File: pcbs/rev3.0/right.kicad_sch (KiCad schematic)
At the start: 31 parts, among them J2 Conn_ST_STDC14, SW66 MK-12C03-G015, U10 GT-TC020A-H035-L05, U6 LDI1117, U7 USBLC6-2SC6_C5261088, U8 358, U9 STM32F446RCTx, Y2 8MHz

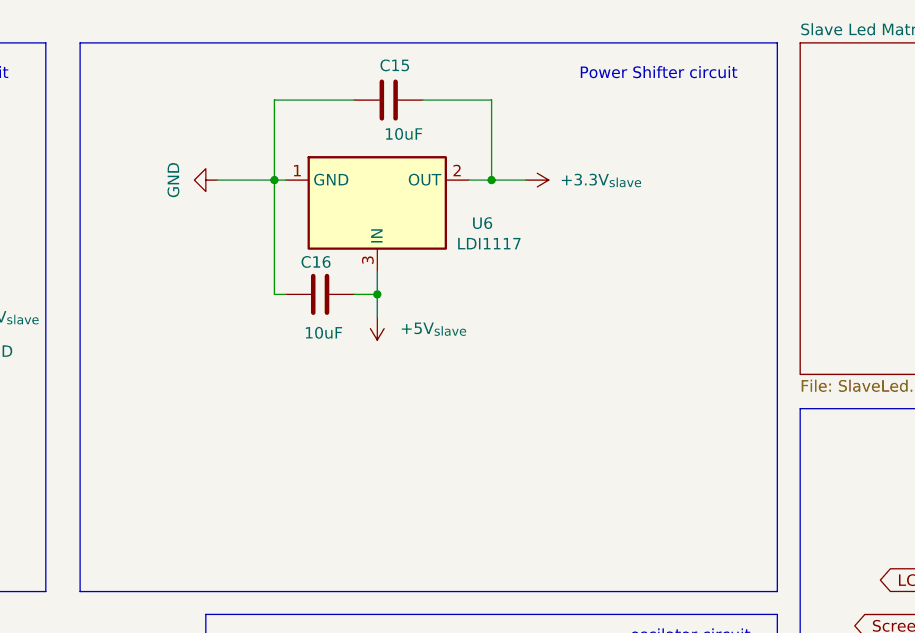
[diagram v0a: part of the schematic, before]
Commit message: Change LDI3.3 LCSC part number to Diotec part
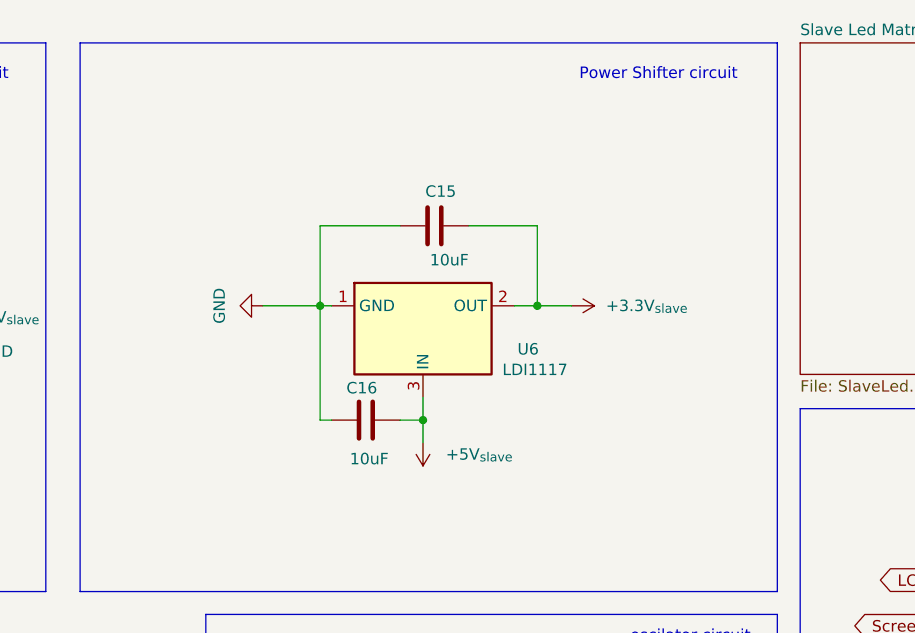
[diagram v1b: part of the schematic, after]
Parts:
- U6: LCSC C6186 -> (none); LCSC Part C6186 -> (none)
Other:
- moved on the sheet: C15, C16, U6
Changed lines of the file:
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@@
 	)
 	(junction
-		(at 157.48 43.18)
+		(at 162.56 57.15)
 		(diameter 0)
 		(color 0 0 0 0)
@@
 	)
 	(junction
-		(at 146.05 30.48)
+		(at 151.13 44.45)
 		(diameter 0)
 		(color 0 0 0 0)
@@
 	)
 	(junction
-		(at 170.18 30.48)
+		(at 175.26 44.45)
 		(diameter 0)
 		(color 0 0 0 0)
@@
 	(wire
 		(pts
-			(xy 157.48 45.72) (xy 157.48 43.18)
+			(xy 162.56 59.69) (xy 162.56 57.15)
 		)
 		(stroke
@@
 	(wire
 		(pts
-			(xy 146.05 43.18) (xy 147.32 43.18)
+			(xy 151.13 57.15) (xy 152.4 57.15)
 		)
 		(stroke
@@
 	(wire
 		(pts
-			(xy 167.64 30.48) (xy 170.18 30.48)
+			(xy 172.72 44.45) (xy 175.26 44.45)
 		)
 		(stroke
@@
 	(wire
 		(pts
-			(xy 146.05 21.59) (xy 146.05 30.48)
+			(xy 151.13 35.56) (xy 151.13 44.45)
 		)
 		(stroke
@@
 	(wire
 		(pts
-			(xy 154.94 21.59) (xy 146.05 21.59)
+			(xy 160.02 35.56) (xy 151.13 35.56)
 		)
 		(stroke
@@
 	(wire
 		(pts
-			(xy 157.48 43.18) (xy 157.48 40.64)
+			(xy 162.56 57.15) (xy 162.56 54.61)
 		)
 		(stroke
@@
 	(wire
 		(pts
-			(xy 170.18 30.48) (xy 170.18 21.59)
+			(xy 175.26 44.45) (xy 175.26 35.56)
 		)
 		(stroke
@@
 	(wire
 		(pts
-			(xy 170.18 21.59) (xy 162.56 21.59)
+			(xy 175.26 35.56) (xy 167.64 35.56)
 		)
 		(stroke
@@
 	(wire
 		(pts
-			(xy 146.05 30.48) (xy 147.32 30.48)
+			(xy 151.13 44.45) (xy 152.4 44.45)
 		)
 		(stroke
@@
 	(wire
 		(pts
-			(xy 139.7 30.48) (xy 146.05 30.48)
+			(xy 144.78 44.45) (xy 151.13 44.45)
 		)
 		(stroke
@@
 	(wire
 		(pts
-			(xy 146.05 30.48) (xy 146.05 43.18)
+			(xy 151.13 44.45) (xy 151.13 57.15)
 		)
 		(stroke
@@
 	(wire
 		(pts
-			(xy 154.94 43.18) (xy 157.48 43.18)
+			(xy 160.02 57.15) (xy 162.56 57.15)
 		)
 		(stroke
@@
 	(wire
 		(pts
-			(xy 170.18 30.48) (xy 173.99 30.48)
+			(xy 175.26 44.45) (xy 179.07 44.45)
 		)
 		(stroke
@@
 	(symbol
 		(lib_id "Device:C")
-		(at 151.13 43.18 90)
+		(at 156.21 57.15 90)
 		(unit 1)
 		(exclude_from_sim no)
@@
 		(dnp no)
 		(property "Reference" "C16"
-			(at 152.4 39.624 90)
+			(at 157.48 53.594 90)
 			(effects
 				(font
@@
 		)
 		(property "Value" "10uF"
-			(at 153.67 47.498 90)
+			(at 158.75 61.468 90)
 			(effects
 				(font
@@
 		)
 		(property "Footprint" "Capacitor_SMD:C_1206_3216Metric"
-			(at 154.94 42.2148 0)
+			(at 160.02 56.1848 0)
 			(effects
 				(font
@@
 		)
 		(property "Datasheet" "~"
-			(at 151.13 43.18 0)
+			(at 156.21 57.15 0)
 			(effects
 				(font
@@
 		)
 		(property "Description" "Unpolarized capacitor"
-			(at 151.13 43.18 0)
+			(at 156.21 57.15 0)
 			(effects
 				(font
@@
 		)
 		(property "LCSC" "C13585"
-			(at 151.13 43.18 0)
+			(at 156.21 57.15 0)
 			(effects
 				(font
@@
 		)
 		(property "LCSC Part" "C13585"
-			(at 151.13 43.18 0)
+			(at 156.21 57.15 0)
 			(effects
 				(font
@@
 	(symbol
 		(lib_id "power:+3.3V")
-		(at 173.99 30.48 270)
+		(at 179.07 44.45 270)
 		(unit 1)
 		(exclude_from_sim no)
@@
 		(fields_autoplaced yes)
 		(property "Reference" "#PWR038"
-			(at 170.18 30.48 0)
+			(at 175.26 44.45 0)
 			(effects
 				(font
@@
 		)
 		(property "Value" "+3.3V_{slave}"
-			(at 177.8 30.4799 90)
+			(at 182.88 44.4499 90)
 			(effects
 				(font
@@
 		)
 		(property "Footprint" ""
-			(at 173.99 30.48 0)
+			(at 179.07 44.45 0)
 			(effects
 				(font
@@
 		)
 		(property "Datasheet" ""
-			(at 173.99 30.48 0)
+			(at 179.07 44.45 0)
 			(effects
 				(font
@@
 		)
 		(property "Description" "Power symbol creates a global label with name \"+3.3V\""
-			(at 173.99 30.48 0)
+			(at 179.07 44.45 0)
 			(effects
 				(font
@@
 	(symbol
 		(lib_id "Regulator_Linear:LT1963AxST-3.3")
-		(at 157.48 33.02 0)
+		(at 162.56 46.99 0)
 		(unit 1)
 		(exclude_from_sim no)
@@
 		(dnp no)
 		(property "Reference" "U6"
-			(at 169.164 35.306 0)
+			(at 174.244 49.276 0)
 			(effects
 				(font
@@
 		)
 		(property "Value" "LDI1117"
-			(at 169.926 37.592 0)
+			(at 175.006 51.562 0)
 			(effects
 				(font
@@
 		)
 		(property "Footprint" "Package_TO_SOT_SMD:SOT-223-3_TabPin2"
-			(at 157.48 44.45 0)
+			(at 162.56 58.42 0)
 			(effects
 				(font
@@
 			)
 		)
-		(property "Datasheet" "https://www.lcsc.com/datasheet/C6186.pdf"
-			(at 157.48 46.99 0)
+		(property "Datasheet" ""
+			(at 162.56 60.96 0)
 			(effects
 				(font
@@
 			)
 		)
-		(property "Description" "Advanced Monolithic Systems AMS1117-3.3"
-			(at 157.48 33.02 0)
+		(property "Description" ""
+			(at 162.56 46.99 0)
 			(effects
 				(font
@@
 			)
 		)
-		(property "LCSC" "C6186"
-			(at 157.48 33.02 0)
+		(property "LCSC" ""
+			(at 162.56 46.99 0)
 			(effects
 				(font
@@
 			)
 		)
-		(property "LCSC Part" "C6186"
-			(at 157.48 33.02 0)
+		(property "LCSC Part" ""
+			(at 162.56 46.99 0)
 			(effects
 				(font
@@
 	(symbol
 		(lib_id "Device:C")
-		(at 158.75 21.59 270)
+		(at 163.83 35.56 270)
 		(unit 1)
 		(exclude_from_sim no)
@@
 		(dnp no)
 		(property "Reference" "C15"
-			(at 157.734 17.78 90)
+			(at 162.814 31.75 90)
 			(effects
 				(font
@@
 		)
 		(property "Value" "10uF"
-			(at 158.242 25.4 90)
+			(at 163.322 39.37 90)
 			(effects
 				(font
@@
 		)
 		(property "Footprint" "Capacitor_SMD:C_1206_3216Metric"
-			(at 154.94 22.5552 0)
+			(at 160.02 36.5252 0)
 			(effects
 				(font
@@
 		)
 		(property "Datasheet" "~"
-			(at 158.75 21.59 0)
+			(at 163.83 35.56 0)
 			(effects
 				(font
@@
 		)
 		(property "Description" "Unpolarized capacitor"
-			(at 158.75 21.59 0)
+			(at 163.83 35.56 0)
 			(effects
 				(font
@@
 		)
 		(property "LCSC" "C13585"
-			(at 158.75 21.59 0)
+			(at 163.83 35.56 0)
 			(effects
 				(font
@@
 		)
 		(property "LCSC Part" "C13585"
-			(at 158.75 21.59 0)
+			(at 163.83 35.56 0)
 			(effects
 				(font
@@
 	(symbol
 		(lib_id "power:+5V")
-		(at 157.48 45.72 180)
+		(at 162.56 59.69 180)
 		(unit 1)
 		(exclude_from_sim no)
@@
 		(fields_autoplaced yes)
 		(property "Reference" "#PWR043"
-			(at 157.48 41.91 0)
+			(at 162.56 55.88 0)
 			(effects
 				(font
@@
 		)
 		(property "Value" "+5V_{slave}"
-			(at 160.02 46.9899 0)
+			(at 165.1 60.9599 0)
 			(effects
 				(font
@@
 		)
 		(property "Footprint" ""
-			(at 157.48 45.72 0)
+			(at 162.56 59.69 0)
 			(effects
 				(font
@@
 		)
 		(property "Datasheet" ""
-			(at 157.48 45.72 0)
+			(at 162.56 59.69 0)
 			(effects
 				(font
@@
 		)
 		(property "Description" "Power symbol creates a global label with name \"+5V\""
-			(at 157.48 45.72 0)
+			(at 162.56 59.69 0)
 			(effects
 				(font
@@
 	(symbol
 		(lib_id "power:GND")
-		(at 139.7 30.48 270)
+		(at 144.78 44.45 270)
 		(unit 1)
 		(exclude_from_sim no)
@@
 		(dnp no)
 		(property "Reference" "#PWR037"
-			(at 133.35 30.48 0)
+			(at 138.43 44.45 0)
 			(effects
 				(font
@@
 		)
 		(property "Value" "GND"
-			(at 134.874 30.48 0)
+			(at 139.954 44.45 0)
 			(effects
 				(font
@@
 		)
 		(property "Footprint" ""
-			(at 139.7 30.48 0)
+			(at 144.78 44.45 0)
 			(effects
 				(font
@@
 		)
 		(property "Datasheet" ""
-			(at 139.7 30.48 0)
+			(at 144.78 44.45 0)
 			(effects
 				(font
@@
 		)
 		(property "Description" "Power symbol creates a global label with name \"GND\" , ground"
-			(at 139.7 30.48 0)
+			(at 144.78 44.45 0)
 			(effects
 				(font
